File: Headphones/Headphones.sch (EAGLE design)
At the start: 3 parts, among them U1 SI4468

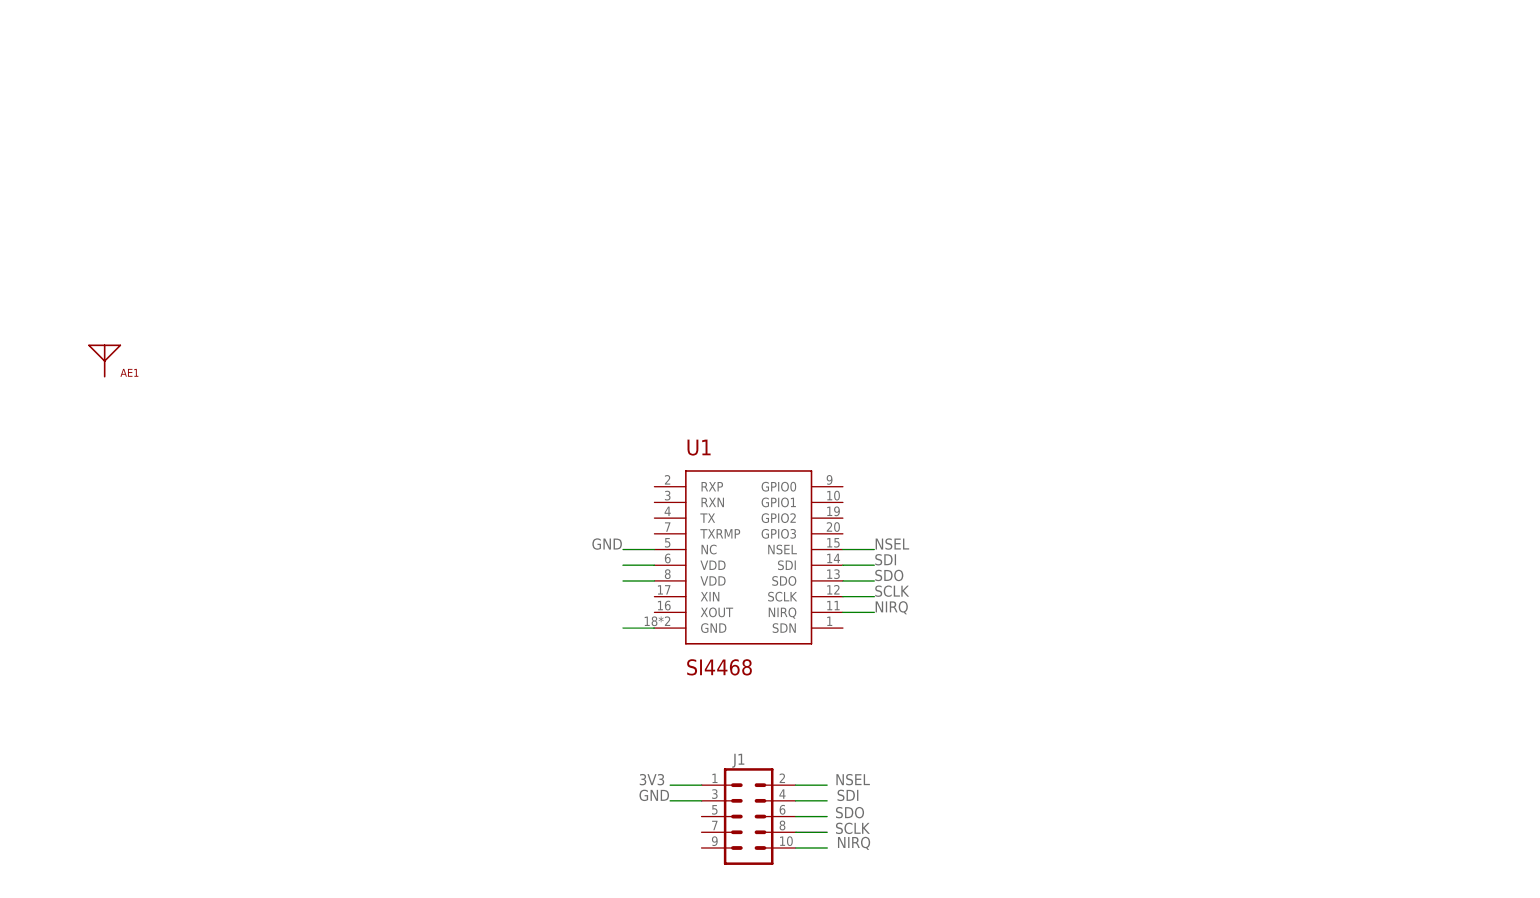
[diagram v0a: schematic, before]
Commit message: Component placement is mostly complete. Need to finish routing
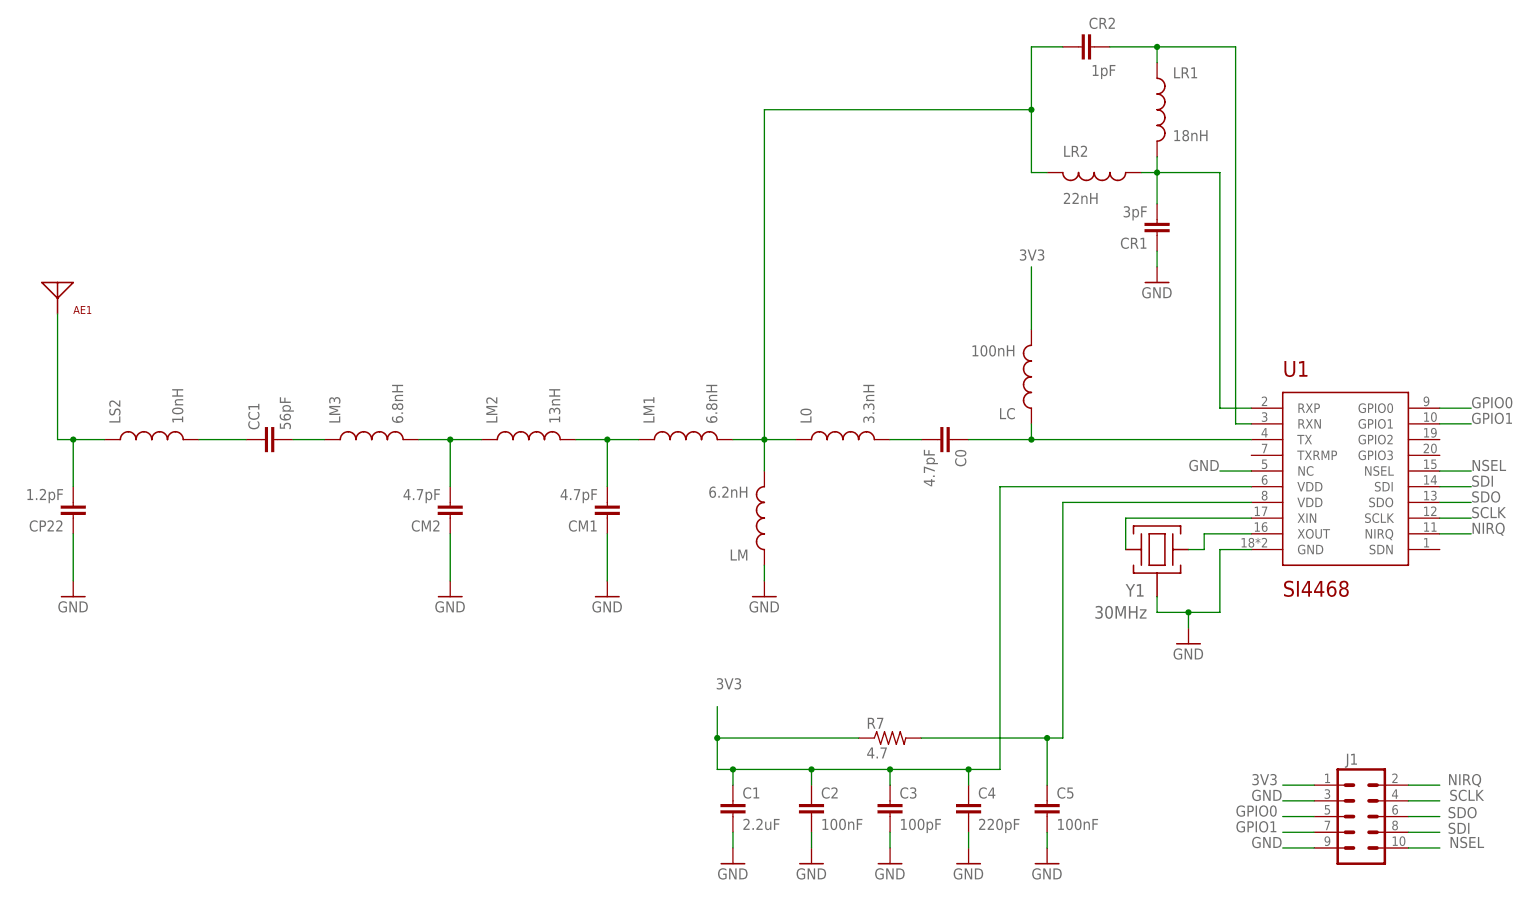
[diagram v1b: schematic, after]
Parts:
- added C0, CM1, CM2: 4.7pF, resistor:C-EUC0603
- added C1: 2.2uF, resistor:C-EUC0603
- added C2, C5: 100nF, resistor:C-EUC0603
- added C3: 100pF, resistor:C-EUC0603
- added C4: 220pF, resistor:C-EUC0603
- added CC1: 56pF, resistor:C-EUC0603
- added CP22: 1.2pF, resistor:C-EUC0603
- added CR1: 3pF, resistor:C-EUC0603
- added CR2: 1pF, resistor:C-EUC0603
- added L0: 3.3nH, SparkFun-Passives:INDUCTOR0603
- added LC: 100nH, SparkFun-Passives:INDUCTOR0603
- added LM: 6.2nH, SparkFun-Passives:INDUCTOR0603
- added LM1, LM3: 6.8nH, SparkFun-Passives:INDUCTOR0603
- added LM2: 13nH, SparkFun-Passives:INDUCTOR0603
- added LR1: 18nH, SparkFun-Passives:INDUCTOR0603
- added LR2: 22nH, SparkFun-Passives:INDUCTOR0603
- added LS2: 10nH, SparkFun-Passives:INDUCTOR0603
- added R7: 4.7, resistor:R-US_R0603
- added Y1: 30MHz, Master:ABM10-30-D30-T3
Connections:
- new net GPIO0: J1.5, U1.GPIO0
- new net GPIO1: J1.7, U1.GPIO1
- new net N$1: U1.XOUT, Y1.1
- new net N$10: C0.1, LC.1, U1.TX
- new net N$11: CM1.2, LM1.1, LM2.2
- new net N$12: CM2.2, LM2.1, LM3.2
- new net N$13: AE1.RF, CP22.2, LS2.1
- new net N$2: U1.XIN, Y1.2
- new net N$3: C0.2, L0.2
- new net N$4: CR2.2, LR1.1, U1.RXN
- new net N$5: CR1.2, LR1.2, LR2.1, U1.RXP
- new net N$6: CR2.1, L0.1, LM.2, LM1.2, LR2.2
- new net N$9: CC1.1, LS2.2
- net 3V3: now also C1.1, C2.1, C3.1, C4.1, LC.2, R7.1, U1.VDD@1
- net GND: now also C1.2, C2.2, C3.2, C4.2, C5.2, CM1.1, CM2.1, CP22.1, CR1.1, J1.9, LM.1, Y1.GND
- net N$7: now also C5.1, R7.2
- net N$8: now also CC1.2, LM3.1; no longer U1.VDD@1
- net NIRQ: now also J1.2; no longer J1.10
- net NSEL: now also J1.10; no longer J1.2
- net SCLK: now also J1.4; no longer J1.8
- net SDI: now also J1.8; no longer J1.4
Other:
- moved on the sheet: AE1, J1, U1

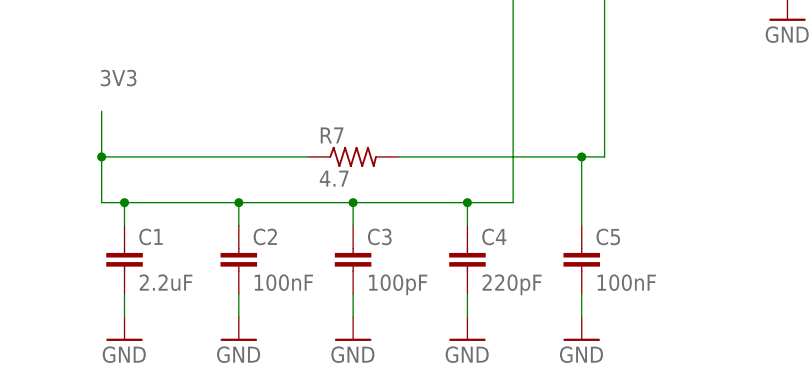
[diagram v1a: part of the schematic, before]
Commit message: Finished most of the layout. Still need to run DRC, ERC, and standardize text
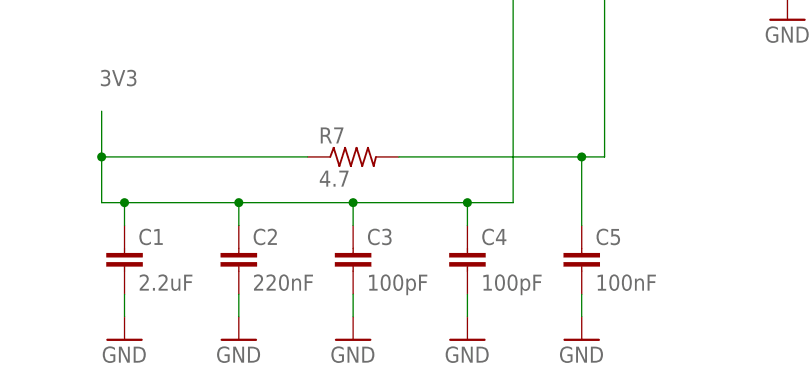
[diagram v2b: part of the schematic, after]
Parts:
- C2: value 100nF -> 220nF
- C4: value 220pF -> 100pF
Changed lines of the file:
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@@
 <class number="0" name="default" width="0" drill="0">
+</class>
+<class number="1" name="50ohm" width="1.26" drill="0">
+<clearance class="1" value="0.25"/>
 </class>
 </classes>
@@
 <part name="J1" library="SparkFun-Connectors" deviceset="M05X2" device="PTH"/>
 <part name="C1" library="resistor" deviceset="C-EU" device="C0603" value="2.2uF"/>
-<part name="C2" library="resistor" deviceset="C-EU" device="C0603" value="100nF"/>
+<part name="C2" library="resistor" deviceset="C-EU" device="C0603" value="220nF"/>
 <part name="C3" library="resistor" deviceset="C-EU" device="C0603" value="100pF"/>
-<part name="C4" library="resistor" deviceset="C-EU" device="C0603" value="220pF"/>
+<part name="C4" library="resistor" deviceset="C-EU" device="C0603" value="100pF"/>
 <part name="C5" library="resistor" deviceset="C-EU" device="C0603" value="100nF"/>
 <part name="CC1" library="resistor" deviceset="C-EU" device="C0603" value="56pF"/>
@@
 </segment>
 </net>
-<net name="N$9" class="0">
+<net name="N$9" class="1">
 <segment>
 <pinref part="LS2" gate="G$1" pin="2"/>
